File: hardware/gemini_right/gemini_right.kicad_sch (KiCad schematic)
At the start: 78 parts, among them IC1 XL9555__TSSOP-24_, IC2 ESP32-C3-WROOM-02-N4, IC3 CW2015CSAC, J1 Conn_01x02_Pin, J1_toLeft USB_C_Receptacle_USB2.0_16P, J2_toHost USB_C_Receptacle_USB2.0_16P, J3_passthrough USB_C_Receptacle_USB2.0_16P, SW1 SW_Push, SW10 SW_Push, SW11 SW_Push, SW12 SW_Push, SW13 SW_Push, SW14 SW_Push, SW15 SW_Push, SW16 SW_Push, SW17 SW_Push, SW18 SW_Push, SW19 SW_Push, SW2 SW_Push, SW3 SW_Push, SW4 SW_Push, SW5 SW_Push, SW6 SW_Push, SW7 SW_Push, SW8 SW_Push, SW9 SW_Push, U1 IP5407, U2 XC6206PxxxMR, U3 CH9329

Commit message: cleanup
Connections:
- net USB_HID_TRANSMIT: now also U3.9 (UP)
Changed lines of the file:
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@@
+		)
+	)
+	(label "USB_HID_TRANSMIT"
+		(at 144.78 172.72 0)
+		(fields_autoplaced yes)
+		(effects
+			(font
+				(size 1.27 1.27)
+			)
+			(justify left bottom)
 		)
 	)

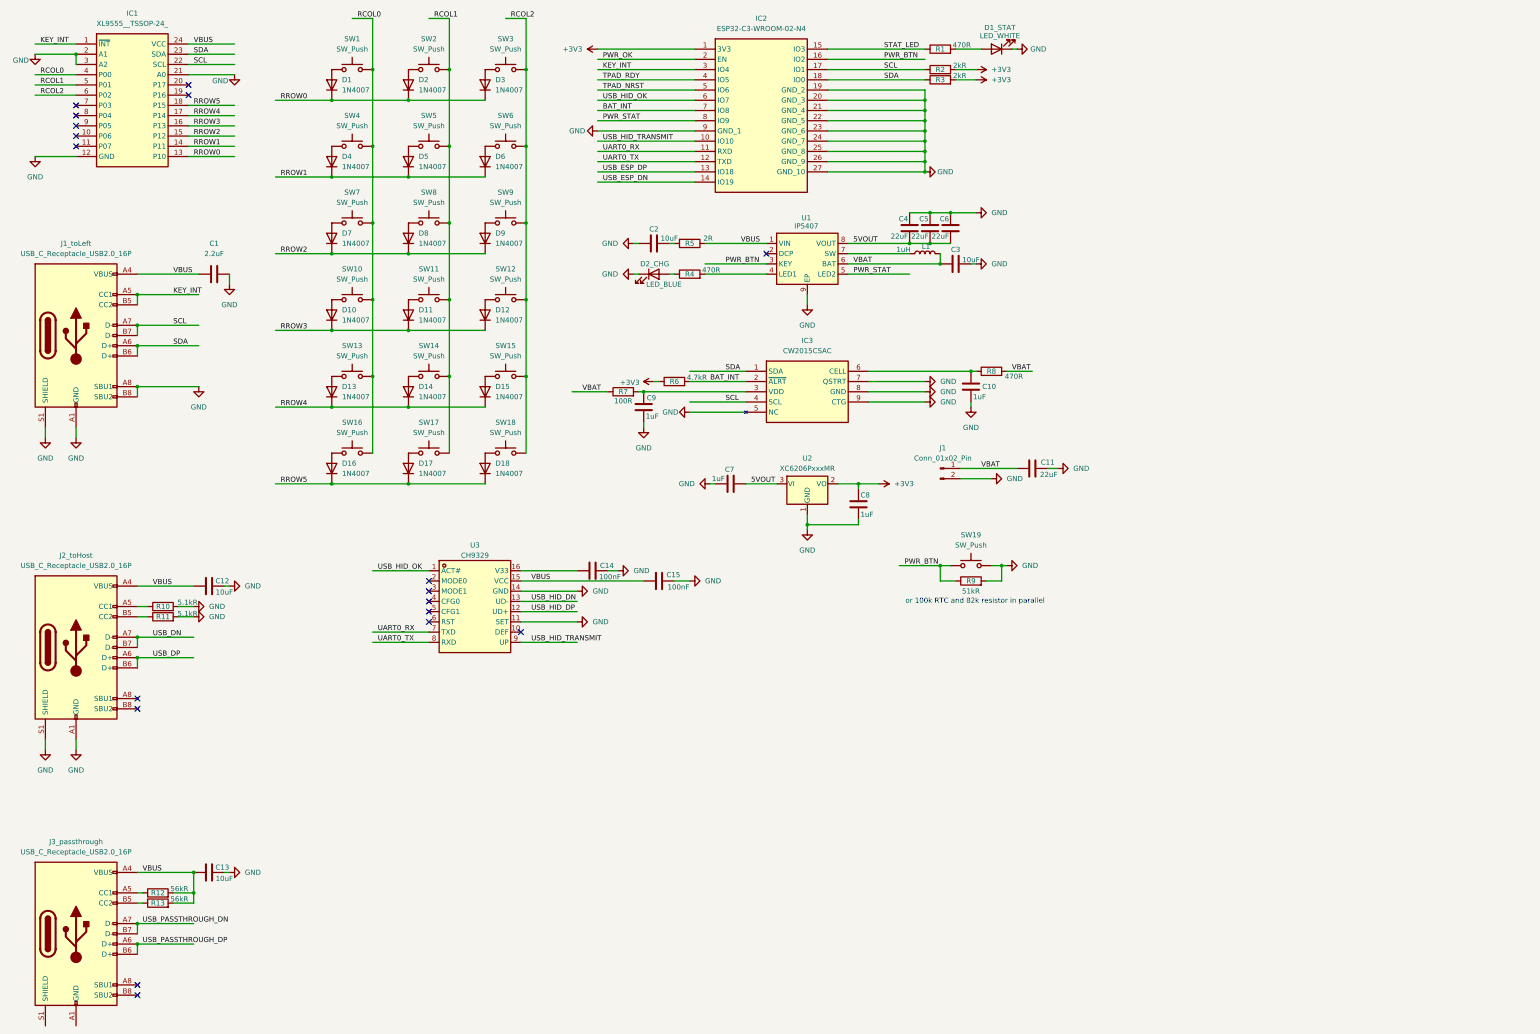
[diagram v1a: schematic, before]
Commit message: initial routing for gemini_right
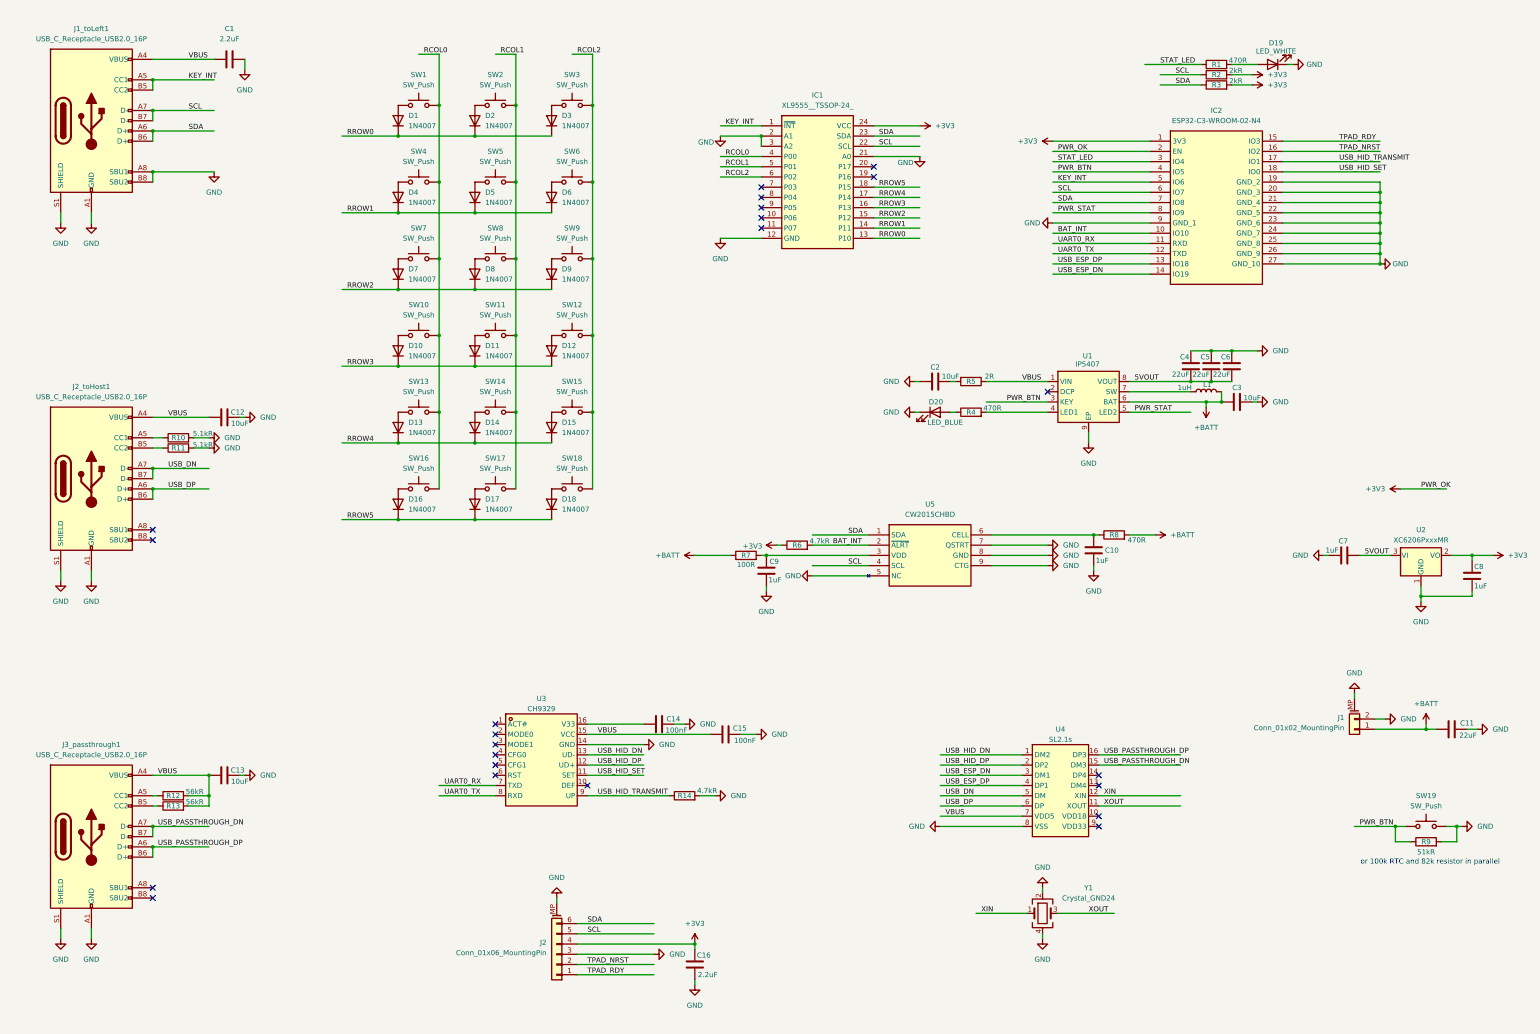
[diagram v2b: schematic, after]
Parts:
- removed D1_STAT: LED_WHITE, symbol Device:LED
- removed IC3: CW2015CSAC, CW2015CSAC, symbol CW2015CSAC:CW2015CSAC
- removed J1: Conn_01x02_Pin, symbol Connector:Conn_01x02_Pin
- added C16: 2.2uF, Capacitor_SMD:C_0603_1608Metric_Pad1.08x0.95mm_HandSolder, symbol Device:C
- added D19: LED_WHITE, Diode_SMD:D_0603_1608Metric_Pad1.05x0.95mm_HandSolder, symbol Device:LED
- added J1: Conn_01x02_MountingPin, mx1.25_1x02_p1.25:CONN-SMD_2P-P1.25_XUNPU_WAFER-MX1.25-2PWB, symbol Connector_Generic_MountingPin:Conn_01x02_MountingPin
- added J2: Conn_01x06_MountingPin, FPC_1x06_p0.5:FPC-SMD_6P-P0.50_XUNPU_FPC-05F-6PH20, symbol Connector_Generic_MountingPin:Conn_01x06_MountingPin
- added R14: 4.7kR, Resistor_SMD:R_0603_1608Metric_Pad0.98x0.95mm_HandSolder, symbol Device:R
- added U4: SL2.1s, ssop-16_L4.6-W2.6-P0.53-LS4.0:SSOP-16_L4.6-W2.6-P0.53-LS4.0-BL, symbol sl2.1s:sl2.1s
- added U5: CW2015CHBD, Package_DFN_QFN:TDFN-8-1EP_3x2mm_P0.5mm_EP1.4x1.4mm, symbol CW2015:CW2015CHBD
- added Y1: Crystal_GND24, Oscillator:Oscillator_SMD_Abracon_ASE-4Pin_3.2x2.5mm_HandSoldering, symbol Device:Crystal_GND24
- C10, C11, C12, C13, C14, C15, C2, C3, C4, C5, C6, C7, C8, C9: footprint (none) -> Capacitor_SMD:C_0603_1608Metric_Pad1.08x0.95mm_HandSolder
- D20: renamed from D2_CHG; footprint (none) -> Diode_SMD:D_0603_1608Metric_Pad1.05x0.95mm_HandSolder
- IC2: footprint ESP32C3WROOM02N4 -> ESP32C3WROOM02N4:ESP32C3WROOM02N4
- J2_toHost1: renamed from J2_toHost; footprint (none) -> Connector_USB:USB_C_Receptacle_GCT_USB4105-xx-A_16P_TopMnt_Horizontal
- J3_passthrough1: renamed from J3_passthrough; footprint (none) -> Connector_USB:USB_C_Receptacle_GCT_USB4105-xx-A_16P_TopMnt_Horizontal
- L1: footprint (none) -> Inductor_SMD:L_Sunlord_MWSA0402S
- R1, R10, R11, R12, R13, R2, R3, R4, R5, R6, R7, R8, R9: footprint (none) -> Resistor_SMD:R_0603_1608Metric_Pad0.98x0.95mm_HandSolder
- SW19: footprint (none) -> Button_Switch_SMD:SW_SPST_SKQG_WithoutStem
- U1: footprint IP5407 -> IP5306_4.35V:SOIC127P600X165-9N
- renumbered J1_toLeft to J1_toLeft1
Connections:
- net PWR_OK is gone; now on net +3V3: IC2.2 (EN)
- net +3V3: now also IC1.24 (VCC), C16.1, J2.4 (Pin_4)
- net BAT_INT: now also IC2.10 (IO10), U5.2 (~{ALRT}); no longer IC2.7 (IO8)
- net GND: now also J3_passthrough1.A1 (GND), J3_passthrough1.A12 (GND), J3_passthrough1.B1 (GND), J3_passthrough1.B12 (GND), J3_passthrough1.S1 (SHIELD), C16.2, D19.1 (K), J1.2 (Pin_2), J1.MP (MountPin), J2.3 (Pin_3), J2.MP (MountPin), R14.2, U4.8 (VSS), U5.5 (NC), U5.7 (QSTRT), U5.8 (GND), U5.9 (CTG), Y1.2, Y1.4; no longer U3.11 (SET)
- net KEY_INT: now also IC2.5 (IO6); no longer IC2.3 (IO4)
- net PWR_BTN: now also IC2.4 (IO5); no longer IC2.16 (IO2)
- net SCL: now also IC2.6 (IO7), J2.5 (Pin_5), U5.4 (SCL); no longer IC2.17 (IO1)
- net SDA: now also IC2.7 (IO8), J2.6 (Pin_6), U5.1 (SDA); no longer IC2.18 (IO0)
- net STAT_LED: now also IC2.3 (IO4); no longer IC2.15 (IO3)
- net TPAD_NRST: now also IC2.16 (IO2), J2.2 (Pin_2); no longer IC2.5 (IO6)
- net TPAD_RDY: now also IC2.15 (IO3), J2.1 (Pin_1); no longer IC2.4 (IO5)
- net USB_DN: now also U4.5 (DM)
- net USB_DP: now also U4.6 (DP)
- net USB_ESP_DN: now also U4.3 (DM1)
- net USB_ESP_DP: now also U4.4 (DP1)
- net USB_HID_DN: now also U4.1 (DM2)
- net USB_HID_DP: now also U4.2 (DP2)
- net USB_HID_TRANSMIT: now also IC2.17 (IO1), R14.1; no longer IC2.10 (IO10)
- net USB_PASSTHROUGH_DN: now also U4.15 (DM3)
- net USB_PASSTHROUGH_DP: now also U4.16 (DP3)
- net VBUS: now also U4.7 (VDD5); no longer IC1.24 (VCC)
- net at R1.2: now also D19.2 (A)
- net at C9.1, R7.2: now also U5.3 (VDD)
- net at C10.1, R8.1: now also U5.6 (CELL)
- net USB_HID_OK: no longer names the net of U3.1 (ACT#)
- net USB_HID_OK: no longer IC2.6 (IO7)
- net VBAT renamed +BATT
- net +BATT: now also J1.1 (Pin_1)
- new net USB_HID_SET: IC2.18 (IO0), U3.11 (SET)
- new net XIN: U4.12 (XIN), Y1.1
- new net XOUT: U4.11 (XOUT), Y1.3
- no-connect marks 18 -> 23
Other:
- moved on the sheet: C1, C10, C11, C12, C13, C14, C15, C2, C3, C4, C5, C6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

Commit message: update schematics
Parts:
- removed C10, C9: 1uF, Capacitor_SMD:C_0603_1608Metric_Pad1.08x0.95mm_HandSolder, symbol Device:C
- removed C13: 10uF, Capacitor_SMD:C_0603_1608Metric_Pad1.08x0.95mm_HandSolder, symbol Device:C
- removed IC2: ESP32-C3-WROOM-02-N4, ESP32C3WROOM02N4:ESP32C3WROOM02N4, symbol ESP32-C3-WROOM-02-N4:ESP32-C3-WROOM-02-N4
- removed J3_passthrough1: USB_C_Receptacle_USB2.0_16P, Connector_USB:USB_C_Receptacle_GCT_USB4105-xx-A_16P_TopMnt_Horizontal, symbol Connector:USB_C_Receptacle_USB2.0_16P
- removed R12, R13: 56kR, Resistor_SMD:R_0603_1608Metric_Pad0.98x0.95mm_HandSolder, symbol Device:R
- removed R14, R6: 4.7kR, Resistor_SMD:R_0603_1608Metric_Pad0.98x0.95mm_HandSolder, symbol Device:R
- removed R5: 2R, Resistor_SMD:R_0603_1608Metric_Pad0.98x0.95mm_HandSolder, symbol Device:R
- removed R7: 100R, Resistor_SMD:R_0603_1608Metric_Pad0.98x0.95mm_HandSolder, symbol Device:R
- removed R8: 470R, Resistor_SMD:R_0603_1608Metric_Pad0.98x0.95mm_HandSolder, symbol Device:R
- removed U1: IP5407, IP5306_4.35V:SOIC127P600X165-9N, symbol ip5407:ip5407
- removed U3: CH9329, sop-16_L9.9-W3.9-P1.27-LS6.0:SOP-16_L9.9-W3.9-P1.27-LS6.0-BL, symbol ch9329:CH9329
- removed U4: SL2.1s, ssop-16_L4.6-W2.6-P0.53-LS4.0:SSOP-16_L4.6-W2.6-P0.53-LS4.0-BL, symbol sl2.1s:sl2.1s
- removed U5: CW2015CHBD, Package_DFN_QFN:TDFN-8-1EP_3x2mm_P0.5mm_EP1.4x1.4mm, symbol CW2015:CW2015CHBD
- removed Y1: Crystal_GND24, Oscillator:Oscillator_SMD_Abracon_ASE-4Pin_3.2x2.5mm_HandSoldering, symbol Device:Crystal_GND24
- added AE1: Antenna_Shield, chxxx:ANT-F-1-2.4G-1.6mmFR4-WCH, symbol Device:Antenna_Shield
- added C12: 0.1uF, Capacitor_SMD:C_0603_1608Metric_Pad1.08x0.95mm_HandSolder, symbol Device:C
- added C7, C8: 1uF, Capacitor_SMD:C_0603_1608Metric_Pad1.08x0.95mm_HandSolder, symbol Device:C
- added IC1: CW2015CHBD, Package_DFN_QFN:TDFN-8-1EP_3x2mm_P0.5mm_EP1.4x1.4mm, symbol CW2015:CW2015CHBD
- added L2: 10uH, Inductor_SMD:L_Chilisin_BMRA00040420, symbol Device:L
- added R10, R2: 470r, Resistor_SMD:R_0603_1608Metric_Pad0.98x0.95mm_HandSolder, symbol Device:R
- added R3: 100r, Resistor_SMD:R_0603_1608Metric_Pad0.98x0.95mm_HandSolder, symbol Device:R
- added SW20: SW_Push, Button_Switch_SMD:SW_Tactile_SPST_NO_Straight_CK_PTS636Sx25SMTRLFS, symbol Switch:SW_Push
- added U1: ETA9742, SOIC127P600X175-9N:SOIC127P600X175-9N, symbol ETA9742:ETA9742
- added U3: CH582F, chxxx:QFN28_4X4, symbol chxxx:CH582F
- added Y1: Crystal, Crystal:Crystal_SMD_3215-2Pin_3.2x1.5mm, symbol Device:Crystal
- added Y2: Crystal_GND24, Crystal:Crystal_SMD_3225-4Pin_3.2x2.5mm_HandSoldering, symbol Device:Crystal_GND24
- C14: value 100nF -> 0.1uF
- C15: value 100nF -> 1uF
- C2, C3: value 10uF -> 22uF
- C4, C6: value 22uF -> 1uF
- D1, D10, D11, D12, D13, D14, D15, D16, D17, D18, D2, D3, D4, D5, D6, D7, D8, D9: footprint Diode_SMD:D_SOD-123F -> Diode_THT:D_DO-41_SOD81_P10.16mm_Horizontal
- D19: footprint Diode_SMD:D_0603_1608Metric_Pad1.05x0.95mm_HandSolder -> LED_SMD:LED_0603_1608Metric_Pad1.05x0.95mm_HandSolder
- D20: value LED_BLUE -> LED_RED; footprint Diode_SMD:D_0603_1608Metric_Pad1.05x0.95mm_HandSolder -> LED_SMD:LED_0603_1608Metric_Pad1.05x0.95mm_HandSolder
- L1: value 1uH -> 2.2uH; footprint Inductor_SMD:L_Sunlord_MWSA0402S -> Inductor_SMD:L_Chilisin_BMRA00040420
- R1: value 470R -> 56k
- R4: value 470R -> 4.7k
- R9: value 51kR -> 470r
- SW19: footprint Button_Switch_SMD:SW_SPST_SKQG_WithoutStem -> Button_Switch_SMD:SW_Tactile_SPST_NO_Straight_CK_PTS636Sx25SMTRLFS
- renumbered C7 to C10, C8 to C11, C16 to C13, C11 to C16, C12 to C9, IC1 to IC2, J2 to J1, J1 to J2, R10 to R5, R11 to R6, R2 to R7, R3 to R8
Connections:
- net +3V3: now also C15.1, R4.1, U3.5 (VIO33/VDD33)
- net +BATT: now also C4.2, C5.2, L1.1, R2.2, R3.2, U1.6 (BAT); no longer C3.1, L1.2
- net 5VOUT: now also C2.1, C3.1, R9.2, R10.2, U1.7 (OUT); no longer C4.1, C5.1, C6.1
- net GND: now also C2.2, C4.1, C5.1, R1.2, AE1.2 (Shield), C12.1, C7.2, C8.1, IC1.1 (CTG), IC1.4 (GND), IC1.6 (QSTRT), IC1.9 (EP), SW20.2, U1.8 (PGND), U1.9 (AGND), U3.0 (GND), Y2.2, Y2.4; no longer C2.1, C4.2, C5.2, D19.1 (K), D20.1 (K), R9.2
- net KEY_INT: now also U3.25 (PA15/MISO/RXD0_/AIN5)
- net PWR_STAT: now also U1.3 (STAT), U3.24 (PA5/TXD3/AIN1)
- net SCL: now also IC1.7 (SCL), U3.10 (PB13/U2D+/SCK0_/SCL/TXD1_)
- net SDA: now also IC1.8 (SDA), U3.11 (PB12/U2D-/SCS_/SDA/RXD1_)
- net STAT_LED: now also D19.1 (K), U3.7 (PA9/TMR0/TXD1/AIN13); no longer R1.1
- net TPAD_NRST: now also U3.27 (PA13/SCK0/PWM5/AIN3)
- net TPAD_RDY: now also U3.26 (PA14/MOSI/TXD0_/AIN4)
- net VBUS: no longer C15.1
- net at D19.2 (A): now also R9.1; no longer R1.2
- net VDCIA: now reaches C14.1
- net VDCIA: now also C12.2, L2.1, U3.22 (VDCIA), U3.3 (VDCID)
- net PWR_ALRT: now reaches R4.2
- net PWR_ALRT: now also IC1.5 (~{ALRT}), U3.28 (PA12/SCS/PWM4/AIN2)
- net at D20.2 (A): now also R10.1; no longer R4.1
- net PWR_BTN renamed ISPn
- net ISPn: now also U3.17 (PB22/TMR3/RXD2_); no longer R9.1
- net USB_DN renamed USB_D-
- net USB_D-: now also U3.13 (PB10/UD-/TMR1_)
- net USB_DP renamed USB_D+
- net USB_D+: now also U3.12 (PB11/UD+/TMR2_)
- new net: C8.2, U3.20 (VINTA)
- new net: AE1.1 (A), U3.21 (ANT)
- new net: R1.1, U1.5 (ISET)
- new net: C6.1, IC1.2 (CELL), R2.1
- new net: L1.2, U1.1 (SW)
- new net: C7.1, IC1.3 (VDD), R3.1
- new net BOOST_STAT: U1.4 (BST), U3.23 (PA4/RXD3/AIN0)
- new net RSTn: SW20.1, U3.16 (PB23/RST/TMR0_/TXD2_/PWM11)
- new net VSW: L2.2, U3.4 (VSW)
- new net WARN_LED: D20.1 (K), U3.6 (PA8/RXD1/AIN12)
- new net X32M_PIN0: U3.19 (X32MI), Y2.3
- new net X32M_PIN1: U3.18 (X32MO), Y2.1
- new net X32k_PIN0: U3.1 (PA11/X32KO/TMR2), Y1.2
- new net X32k_PIN1: U3.2 (PA10/X32KI/TMR1), Y1.1
- no-connect marks 23 -> 14
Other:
- note removed: "or 100k RTC and 82k resistor in parallel"
- moved on the sheet: C10, C11, C13, C16, IC2, J1, J2, R7, R8, U2

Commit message: partially finish layout of new design
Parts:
- removed C5: 22uF, Capacitor_SMD:C_0603_1608Metric_Pad1.08x0.95mm_HandSolder, symbol Device:C
- added R11: 2kR, Resistor_SMD:R_0603_1608Metric_Pad0.98x0.95mm_HandSolder, symbol Device:R
- AE1: footprint chxxx:ANT-F-1-2.4G-1.6mmFR4-WCH -> chxxx_antenna:ANT-F-3-2.4G-1.6mmFR4-WCH_mirror
- D1, D10, D11, D12, D13, D14, D15, D16, D17, D18, D2, D3, D4, D5, D6, D7, D8, D9: footprint Diode_THT:D_DO-41_SOD81_P10.16mm_Horizontal -> Diode_SMD:D_SOD-123F
- Y1: value Crystal -> 32.768khz 12.5pF 20ppm
- Y2: value Crystal_GND24 -> 32Mhz 12pF 10ppm; footprint Crystal:Crystal_SMD_3225-4Pin_3.2x2.5mm_HandSoldering -> Crystal:Crystal_SMD_3225-4Pin_3.2x2.5mm
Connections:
- net 5VOUT is gone; now on net VBUS: C10.2, C2.1, C3.1, R10.2, R9.2, U1.7 (OUT), U2.3 (VI)
- net +3V3: now also C1.1, J1_toLeft1.A4 (VBUS), J1_toLeft1.A9 (VBUS), J1_toLeft1.B4 (VBUS), J1_toLeft1.B9 (VBUS), R11.2
- net BOOST_STAT: now also U3.27 (PA13/SCK0/PWM5/AIN3); no longer U3.23 (PA4/RXD3/AIN0)
- net KEY_INT: now also U3.7 (PA9/TMR0/TXD1/AIN13), R11.1; no longer U3.25 (PA15/MISO/RXD0_/AIN5)
- net PWR_ALRT: now also U3.14 (PB7/TXD0/PWM9); no longer U3.28 (PA12/SCS/PWM4/AIN2)
- net PWR_STAT: now also U3.28 (PA12/SCS/PWM4/AIN2); no longer U3.24 (PA5/TXD3/AIN1)
- net STAT_LED: now also U3.26 (PA14/MOSI/TXD0_/AIN4); no longer U3.7 (PA9/TMR0/TXD1/AIN13)
- net TPAD_NRST: now also U3.8 (PB15/TCK/MISO_/DTR_); no longer U3.27 (PA13/SCK0/PWM5/AIN3)
- net TPAD_RDY: now also U3.9 (PB14/TIO/DSR_/MOSI_/PWM10); no longer U3.26 (PA14/MOSI/TXD0_/AIN4)
- net VBUS: no longer C1.1, J1_toLeft1.A4 (VBUS), J1_toLeft1.A9 (VBUS), J1_toLeft1.B4 (VBUS), J1_toLeft1.B9 (VBUS)
- net WARN_LED: now also U3.25 (PA15/MISO/RXD0_/AIN5); no longer U3.6 (PA8/RXD1/AIN12)
- net ANT: now reaches AE1.1 (A), U3.21 (ANT)

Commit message: finish routing for right half
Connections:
- net PWR_ALRT: now also U3.8 (PB15/TCK/MISO_/DTR_); no longer U3.14 (PB7/TXD0/PWM9)
- net TPAD_NRST: now also U3.14 (PB7/TXD0/PWM9); no longer U3.8 (PB15/TCK/MISO_/DTR_)
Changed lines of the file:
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@@
+		)
+	)
+	(label "TPAD_NRST"
+		(at 378.46 151.13 0)
+		(fields_autoplaced yes)
+		(effects
+			(font
+				(size 1.27 1.27)
+			)
+			(justify left bottom)
 		)
 	)
@@
 	(label "PWR_STAT"
 		(at 296.545 43.18 0)
-		(fields_autoplaced yes)
-		(effects
-			(font
-				(size 1.27 1.27)
-			)
-			(justify left bottom)
-		)
-	)
-	(label "TPAD_NRST"
-		(at 378.46 166.37 0)
 		(fields_autoplaced yes)
 		(effects
@@
 		)
 	)
-	(label "PWR_ALRT"
-		(at 378.46 151.13 0)
-		(fields_autoplaced yes)
-		(effects
-			(font
-				(size 1.27 1.27)
-			)
-			(justify left bottom)
-		)
-	)
 	(label "X32k_PIN0"
 		(at 313.69 208.28 0)
@@
 		(fields_autoplaced yes)
 		(effects
+			(font
+				(size 1.27 1.27)
+			)
+			(justify left bottom)
+		)
+	)
+	(label "PWR_ALRT"
+		(at 378.46 166.37 0)
+		(fields_autoplaced yes)
+		(effects

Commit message: update capacitor
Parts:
- C14: value 0.1uF -> 2.2uF
- C15: value 1uF -> 2.2uF
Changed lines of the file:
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@@
 			)
 		)
-		(property "Value" "0.1uF"
+		(property "Value" "2.2uF"
 			(at 276.225 219.71 0)
 			(effects
@@
 			)
 		)
-		(property "Value" "1uF"
+		(property "Value" "2.2uF"
 			(at 341.63 220.9799 0)
 			(effects
